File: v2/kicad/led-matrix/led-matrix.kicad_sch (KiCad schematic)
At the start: 6 parts

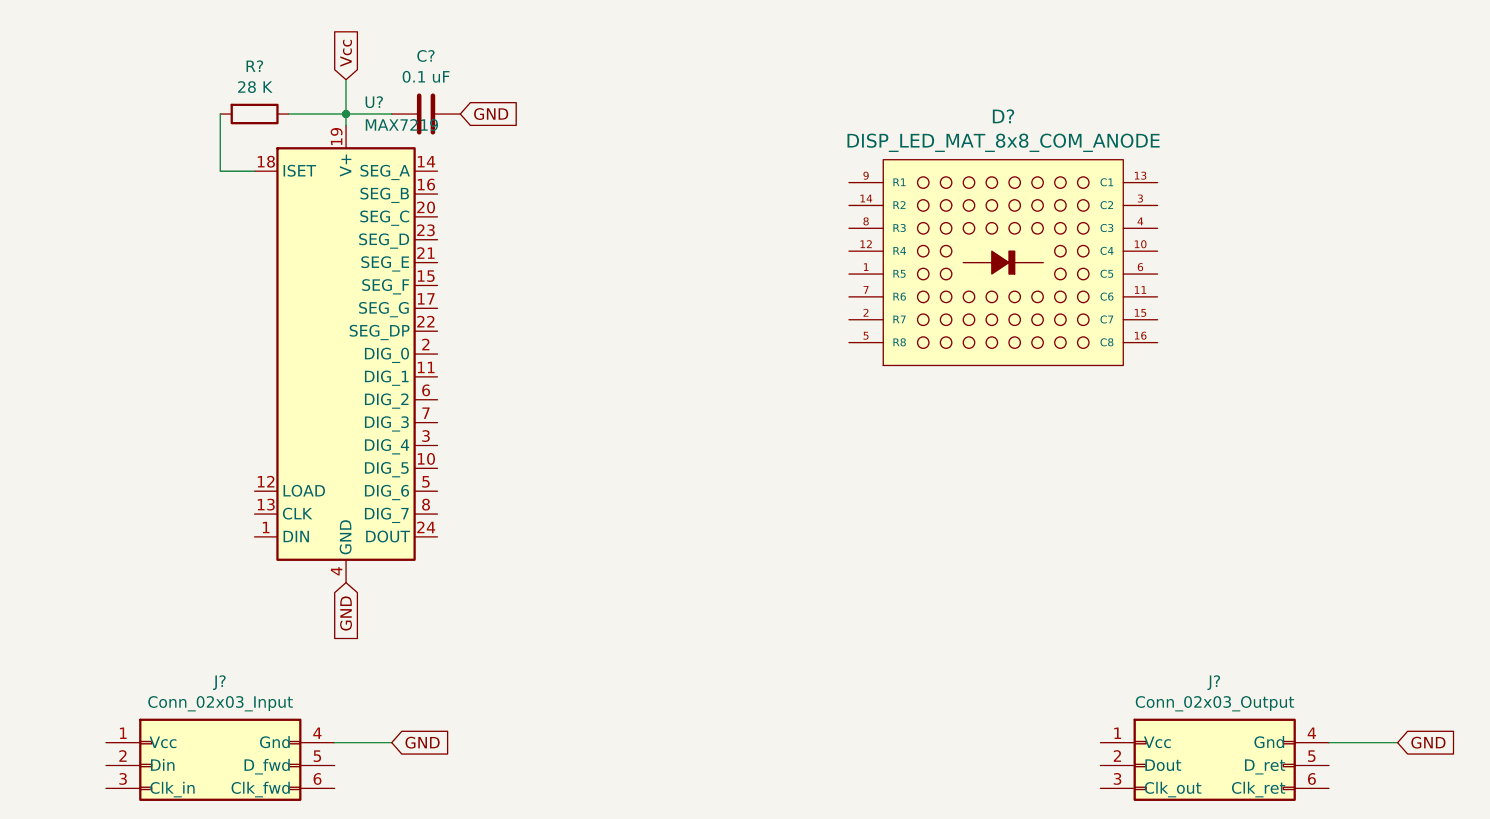
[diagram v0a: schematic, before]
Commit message: v2: KiCAD: Update schematic names, datasheet
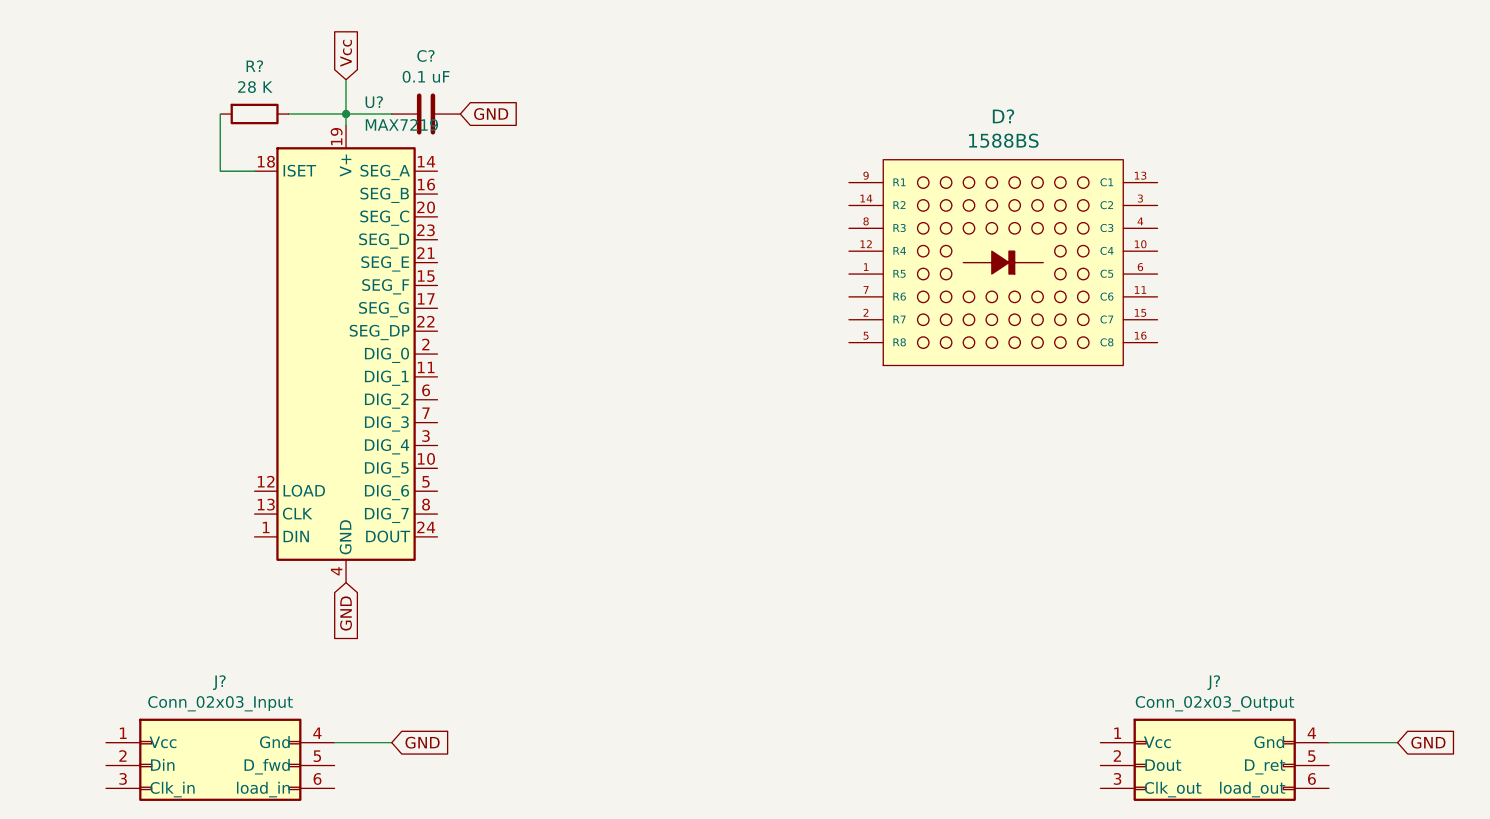
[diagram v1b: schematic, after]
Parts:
- D?: value DISP_LED_MAT_8x8_COM_ANODE -> 1588BS
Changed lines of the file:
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@@
       (effects (font (size 1.524 1.524)))
     )
-    (property "Value" "DISP_LED_MAT_8x8_COM_ANODE" (id 1) (at 125.095 27.1526 0)
+    (property "Value" "1588BS" (id 1) (at 125.095 27.1526 0)
       (effects (font (size 1.524 1.524)))
     )
@@
       (effects (font (size 1.524 1.524)))
     )
-    (property "Datasheet" "" (id 3) (at 110.49 53.34 0)
-      (effects (font (size 1.524 1.524)))
+    (property "Datasheet" "https://www.kingbrightusa.com/images/catalog/SPEC/TC15-11SRWA.pdf" (id 3) (at 110.49 53.34 0)
+      (effects (font (size 1.524 1.524)) hide)
     )
     (pin "9")
@@
     )
     (path "/00000000-0000-0000-0000-000061cd0fa8"
-      (reference "D?") (unit 1) (value "DISP_LED_MAT_8x8_COM_ANODE") (footprint "")
+      (reference "D?") (unit 1) (value "1588BS") (footprint "")
     )
     (path "/00000000-0000-0000-0000-000061d0c670"

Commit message: v2: KiCAD: Add labels vcc, load
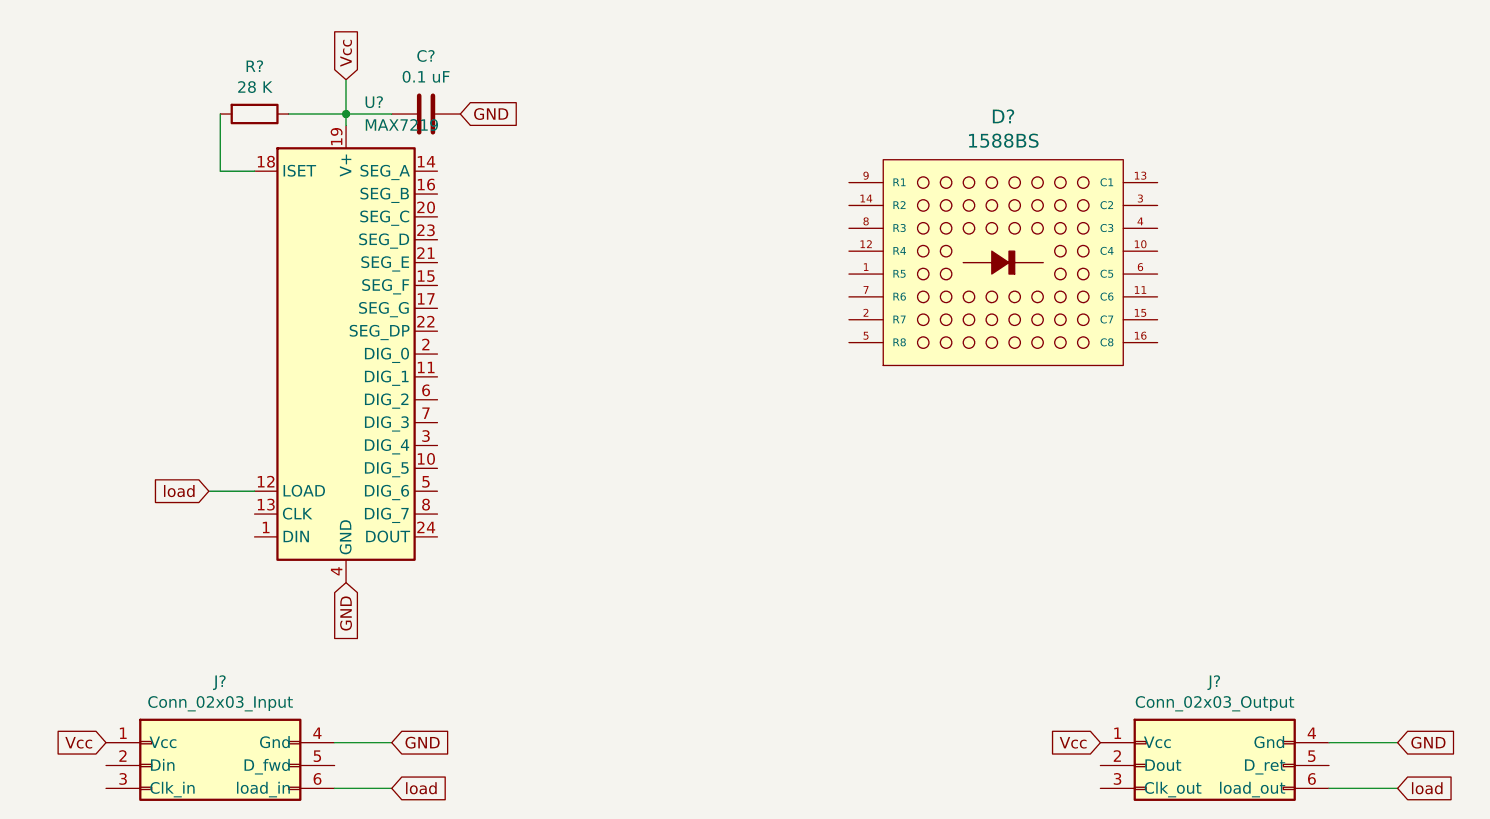
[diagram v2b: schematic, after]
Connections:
- net Vcc: now also J?.1 (Vcc), J?.1 (Vcc)
- net load: now reaches J?.6 (load_in)
- net load: now also J?.6 (load_out), U?.12 (LOAD)
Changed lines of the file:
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@@
   (junction (at 52.07 24.13) (diameter 0) (color 0 0 0 0)
+  )
+  (wire (pts (xy 50.8 99.06) (xy 57.15 99.06))
+    (stroke (width 0) (type default) (color 0 0 0 0))
   )
   (wire (pts (xy 52.07 20.32) (xy 52.07 24.13))
@@
     (stroke (width 0) (type default) (color 0 0 0 0))
   )
+  (wire (pts (xy 161.29 99.06) (xy 168.91 99.06))
+    (stroke (width 0) (type default) (color 0 0 0 0))
+  )
   (wire (pts (xy 45.72 24.13) (xy 52.07 24.13))
     (stroke (width 0) (type default) (color 0 0 0 0))
@@
   )
   (wire (pts (xy 50.8 93.98) (xy 57.15 93.98))
+    (stroke (width 0) (type default) (color 0 0 0 0))
+  )
+  (wire (pts (xy 36.83 66.04) (xy 41.91 66.04))
     (stroke (width 0) (type default) (color 0 0 0 0))
   )
@@
     )
   )
+  (global_label "load" (shape input) (at 168.91 99.06 0) (fields_autoplaced)
+    (effects (font (size 1.27 1.27)) (justify left))
+    (property "Intersheet References" "${INTERSHEET_REFS}" (id 0) (at 175.3466 98.9806 0)
+      (effects (font (size 1.27 1.27)) (justify left) hide)
+    )
+  )
+  (global_label "load" (shape input) (at 57.15 99.06 0) (fields_autoplaced)
+    (effects (font (size 1.27 1.27)) (justify left))
+    (property "Intersheet References" "${INTERSHEET_REFS}" (id 0) (at 63.5866 98.9806 0)
+      (effects (font (size 1.27 1.27)) (justify left) hide)
+    )
+  )
   (global_label "GND" (shape input) (at 52.07 76.2 270) (fields_autoplaced)
     (effects (font (size 1.27 1.27)) (justify right))
@@
     )
   )
+  (global_label "Vcc" (shape input) (at 25.4 93.98 180) (fields_autoplaced)
+    (effects (font (size 1.27 1.27)) (justify right))
+    (property "Intersheet References" "${INTERSHEET_REFS}" (id 0) (at 19.8101 93.9006 0)
+      (effects (font (size 1.27 1.27)) (justify right) hide)
+    )
+  )
+  (global_label "load" (shape input) (at 36.83 66.04 180) (fields_autoplaced)
+    (effects (font (size 1.27 1.27)) (justify right))
+    (property "Intersheet References" "${INTERSHEET_REFS}" (id 0) (at 30.3934 65.9606 0)
+      (effects (font (size 1.27 1.27)) (justify right) hide)
+    )
+  )
   (global_label "GND" (shape input) (at 57.15 93.98 0) (fields_autoplaced)
     (effects (font (size 1.27 1.27)) (justify left))
@@
     )
   )
+  (global_label "Vcc" (shape input) (at 135.89 93.98 180) (fields_autoplaced)
+    (effects (font (size 1.27 1.27)) (justify right))
+    (property "Intersheet References" "${INTERSHEET_REFS}" (id 0) (at 130.3001 93.9006 0)
+      (effects (font (size 1.27 1.27)) (justify right) hide)
+    )
+  )

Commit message: v2: KiCAD: Finish schematic
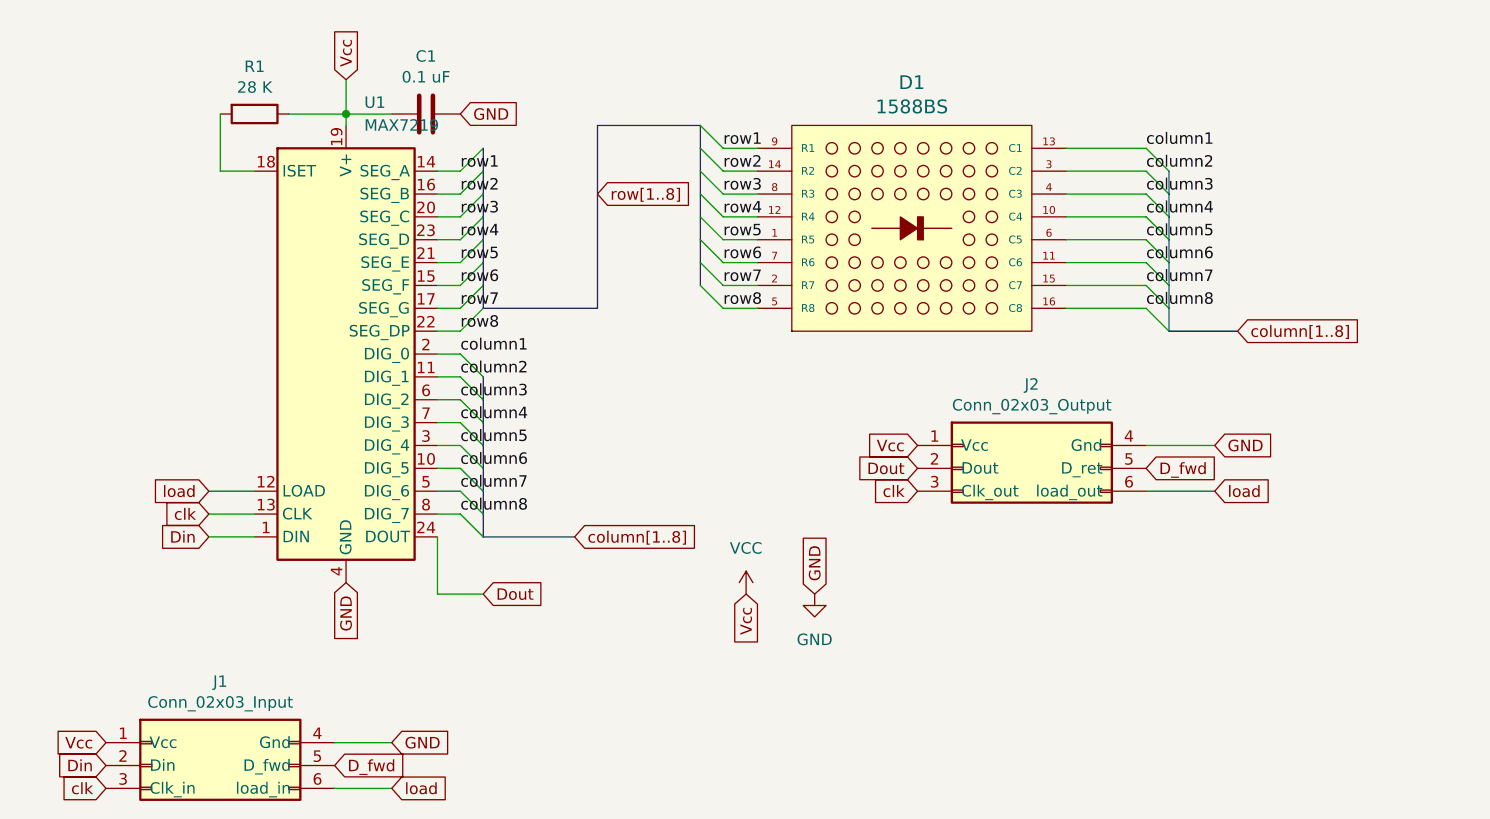
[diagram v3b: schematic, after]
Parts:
- removed U?: MAX7219, symbol Driver_LED:MAX7219
- added U1: MAX7219, symbol my_connectors:MAX7219
- gave numbers to parts that had none: 5
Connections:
- net GND: now also U1.4 (GND), U1.9 (GND)
- net load: now also U1.12 (LOAD)
- net row5: now reaches D1.1 (R5)
- net row5: now also U1.21 (SEG_E)
- net column4: now reaches D1.10 (C4)
- net column4: now also U1.7 (DIG_3)
- net column6: now reaches D1.11 (C6)
- net column6: now also U1.10 (DIG_5)
- net row4: now reaches D1.12 (R4)
- net row4: now also U1.23 (SEG_D)
- net column1: now reaches D1.13 (C1)
- net column1: now also U1.2 (DIG_0)
- net row2: now reaches D1.14 (R2)
- net row2: now also U1.16 (SEG_B)
- net column7: now reaches D1.15 (C7)
- net column7: now also U1.5 (DIG_6)
- net column8: now reaches D1.16 (C8)
- net column8: now also U1.8 (DIG_7)
- net row7: now reaches D1.2 (R7)
- net row7: now also U1.17 (SEG_G)
- net column2: now reaches D1.3 (C2)
- net column2: now also U1.11 (DIG_1)
- net column3: now reaches D1.4 (C3)
- net column3: now also U1.6 (DIG_2)
- net row8: now reaches D1.5 (R8)
- net row8: now also U1.22 (SEG_DP)
- net column5: now reaches D1.6 (C5)
- net column5: now also U1.3 (DIG_4)
- net row6: now reaches D1.7 (R6)
- net row6: now also U1.15 (SEG_F)
- net row3: now reaches D1.8 (R3)
- net row3: now also U1.20 (SEG_C)
- net row1: now reaches D1.9 (R1)
- net row1: now also U1.14 (SEG_A)
- net Din: now reaches J1.2 (Din)
- net Din: now also U1.1 (DIN)
- net clk: now reaches J1.3 (Clk_in)
- net clk: now also J2.3 (Clk_out), U1.13 (CLK)
- net D_fwd: now reaches J1.5 (D_fwd)
- net D_fwd: now also J2.5 (D_ret)
- net Dout: now reaches J2.2 (Dout)
- net Dout: now also U1.24 (DOUT)
- net at R1.2: now also U1.18 (ISET)
- net Vcc renamed VCC
- net VCC: now also U1.19 (V+)
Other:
- moved on the sheet: D1, J2

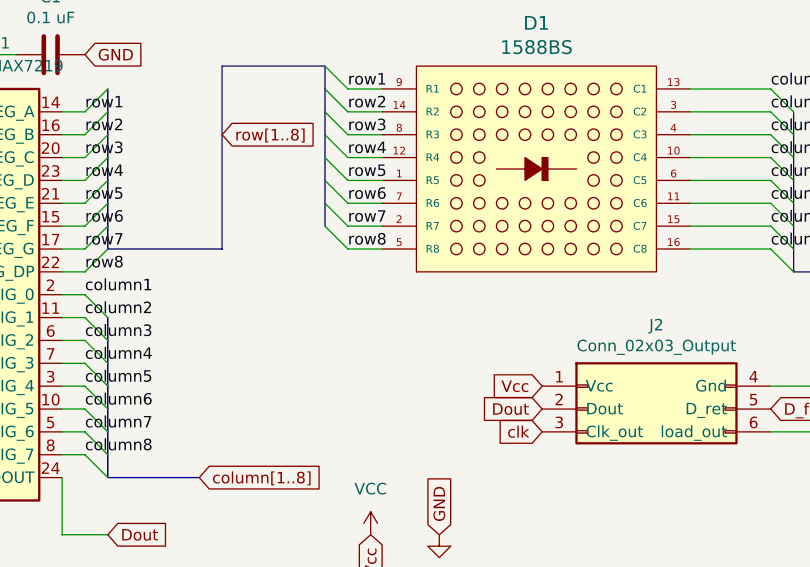
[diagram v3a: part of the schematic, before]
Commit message: v2: Introduce led_matrix footprint, add footprints to schematic
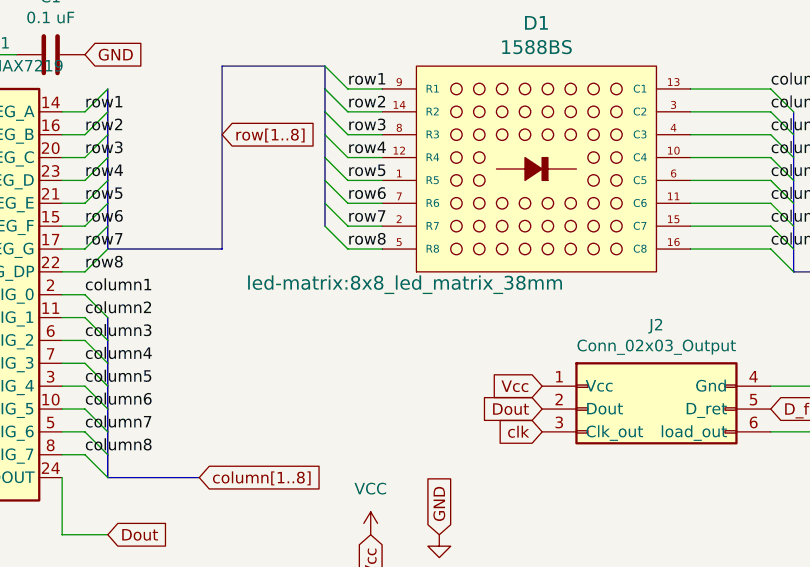
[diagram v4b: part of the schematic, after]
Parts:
- C1: footprint (none) -> Capacitor_SMD:C_1206_3216Metric_Pad1.33x1.80mm_HandSolder
- D1: footprint (none) -> led-matrix:8x8_led_matrix_38mm
- J1: footprint (none) -> Connector_PinSocket_2.54mm:PinSocket_2x03_P2.54mm_Horizontal
- J2: footprint (none) -> Connector_PinHeader_2.54mm:PinHeader_2x03_P2.54mm_Horizontal
- R1: footprint (none) -> Resistor_SMD:R_1206_3216Metric_Pad1.30x1.75mm_HandSolder
- U1: footprint (none) -> Package_SO:SOIC-24W_7.5x15.4mm_P1.27mm
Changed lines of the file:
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@@
       (effects (font (size 1.524 1.524)))
     )
-    (property "Footprint" "" (id 2) (at 100.33 49.53 0)
+    (property "Footprint" "led-matrix:8x8_led_matrix_38mm" (id 2) (at 100.33 49.53 0)
       (effects (font (size 1.524 1.524)))
     )
@@
     (property "Reference" "J1" (id 0) (at 38.1 87.1982 0))
     (property "Value" "Conn_02x03_Input" (id 1) (at 38.1 89.5096 0))
-    (property "Footprint" "" (id 2) (at 30.48 96.52 0)
+    (property "Footprint" "Connector_PinSocket_2.54mm:PinSocket_2x03_P2.54mm_Horizontal" (id 2) (at 30.48 96.52 0)
       (effects (font (size 1.27 1.27)) hide)
     )
@@
     (property "Reference" "J2" (id 0) (at 128.27 54.1782 0))
     (property "Value" "Conn_02x03_Output" (id 1) (at 128.27 56.4896 0))
-    (property "Footprint" "" (id 2) (at 120.65 63.5 0)
+    (property "Footprint" "Connector_PinHeader_2.54mm:PinHeader_2x03_P2.54mm_Horizontal" (id 2) (at 120.65 63.5 0)
       (effects (font (size 1.27 1.27)) hide)
     )
@@
     (property "Reference" "R1" (id 0) (at 41.91 18.8722 90))
     (property "Value" "28 K" (id 1) (at 41.91 21.1836 90))
-    (property "Footprint" "" (id 2) (at 41.91 22.352 90)
+    (property "Footprint" "Resistor_SMD:R_1206_3216Metric_Pad1.30x1.75mm_HandSolder" (id 2) (at 41.91 22.352 90)
       (effects (font (size 1.27 1.27)) hide)
     )
@@
     (property "Reference" "C1" (id 0) (at 60.96 17.7292 90))
     (property "Value" "0.1 uF" (id 1) (at 60.96 20.0406 90))
-    (property "Footprint" "" (id 2) (at 57.15 25.0952 0)
+    (property "Footprint" "Capacitor_SMD:C_1206_3216Metric_Pad1.33x1.80mm_HandSolder" (id 2) (at 57.15 25.0952 0)
       (effects (font (size 1.27 1.27)) hide)
     )
@@
       (effects (font (size 1.27 1.27)) (justify left))
     )
-    (property "Footprint" "" (id 2) (at 50.8 49.53 0)
+    (property "Footprint" "Package_SO:SOIC-24W_7.5x15.4mm_P1.27mm" (id 2) (at 50.8 49.53 0)
       (effects (font (size 1.27 1.27)) hide)
     )
@@
     )
     (path "/00000000-0000-0000-0000-000061d15cc5"
-      (reference "C1") (unit 1) (value "0.1 uF") (footprint "")
+      (reference "C1") (unit 1) (value "0.1 uF") (footprint "Capacitor_SMD:C_1206_3216Metric_Pad1.33x1.80mm_HandSolder")
     )
     (path "/00000000-0000-0000-0000-000061cd0fa8"
-      (reference "D1") (unit 1) (value "1588BS") (footprint "")
+      (reference "D1") (unit 1) (value "1588BS") (footprint "led-matrix:8x8_led_matrix_38mm")
     )
     (path "/00000000-0000-0000-0000-000061d0c670"
-      (reference "J1") (unit 1) (value "Conn_02x03_Input") (footprint "")
+      (reference "J1") (unit 1) (value "Conn_02x03_Input") (footprint "Connector_PinSocket_2.54mm:PinSocket_2x03_P2.54mm_Horizontal")
     )
     (path "/00000000-0000-0000-0000-000061d0dd4c"
-      (reference "J2") (unit 1) (value "Conn_02x03_Output") (footprint "")
+      (reference "J2") (unit 1) (value "Conn_02x03_Output") (footprint "Connector_PinHeader_2.54mm:PinHeader_2x03_P2.54mm_Horizontal")
     )
     (path "/00000000-0000-0000-0000-000061d1432e"
-      (reference "R1") (unit 1) (value "28 K") (footprint "")
+      (reference "R1") (unit 1) (value "28 K") (footprint "Resistor_SMD:R_1206_3216Metric_Pad1.30x1.75mm_HandSolder")
     )
     (path "/82db4006-3899-43e0-b593-d936c945d657"
-      (reference "U1") (unit 1) (value "MAX7219") (footprint "")
+      (reference "U1") (unit 1) (value "MAX7219") (footprint "Package_SO:SOIC-24W_7.5x15.4mm_P1.27mm")
     )
   )
